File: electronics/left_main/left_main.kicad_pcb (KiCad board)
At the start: 4 copper layers, 45 x 51 mm, 186 parts, among them IC1 AS3435-EQFM, IC2 AS3435-EQFM, J1 connectors_board, J10 right_side, J11 right_side, J12 right_side, J13 right_side, J14 right_side, J15 right_side, J16 right_side, J17 right_side, J18 right_side, J19 ear_sensor, J20 ear_sensor, J21 ear_sensor, J3 FF_MIC_L_+, J4 FF_MIC_L_-, J5 FB_MIC_L_+, J6 FB_MIC_L_-, J7 HP_L_+, J8 HP_L_-, J9 right_side, SW2 reset_button, U1 BM83, U2 ATSAMD21G18_QFN, U3 MCP73831T-2ACI/OT, U4 SPX3819-3.3, U5 MAX17048G+T10, U6 AP2127K-1.8, U7 AP22814AW5, U8 AP22814AW5, Y1 32.768KHz

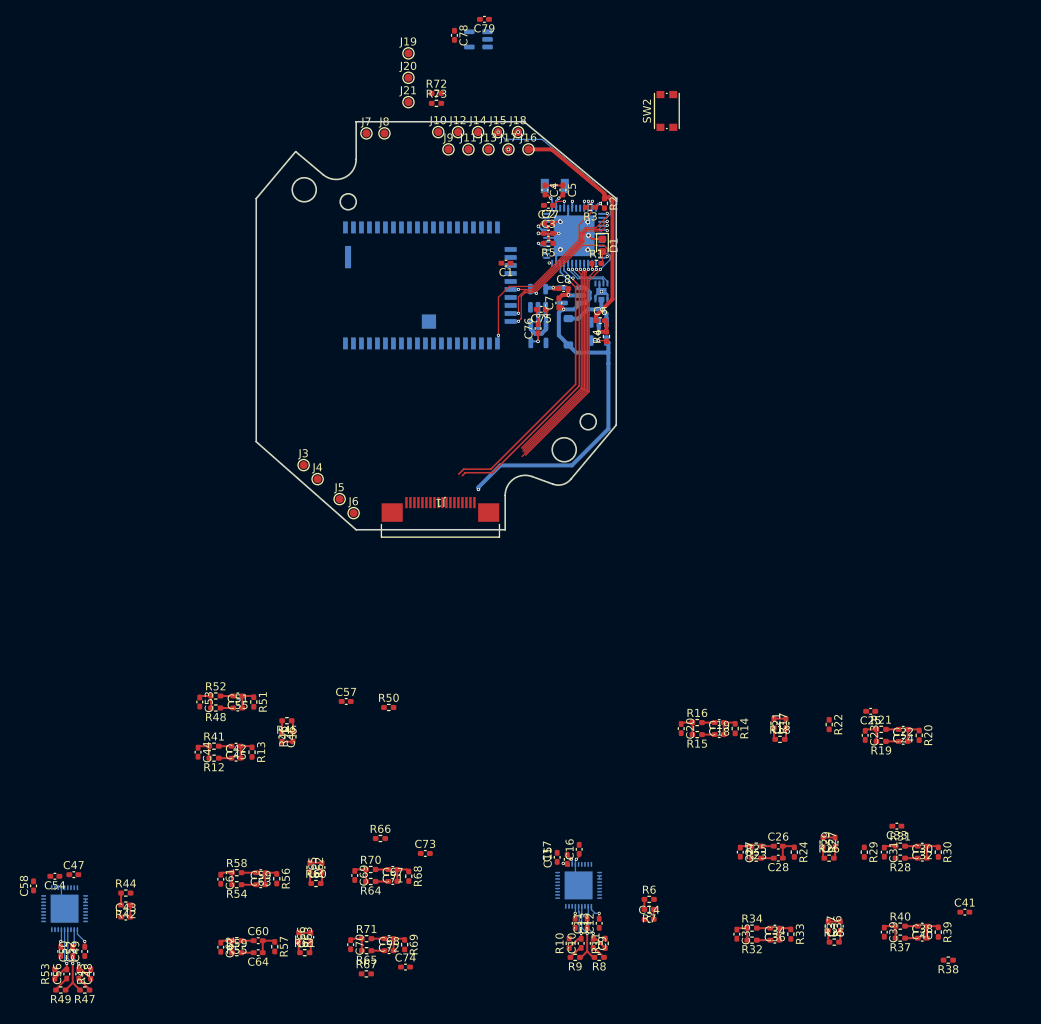
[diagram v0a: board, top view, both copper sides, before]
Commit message: L filterers + drivers layout
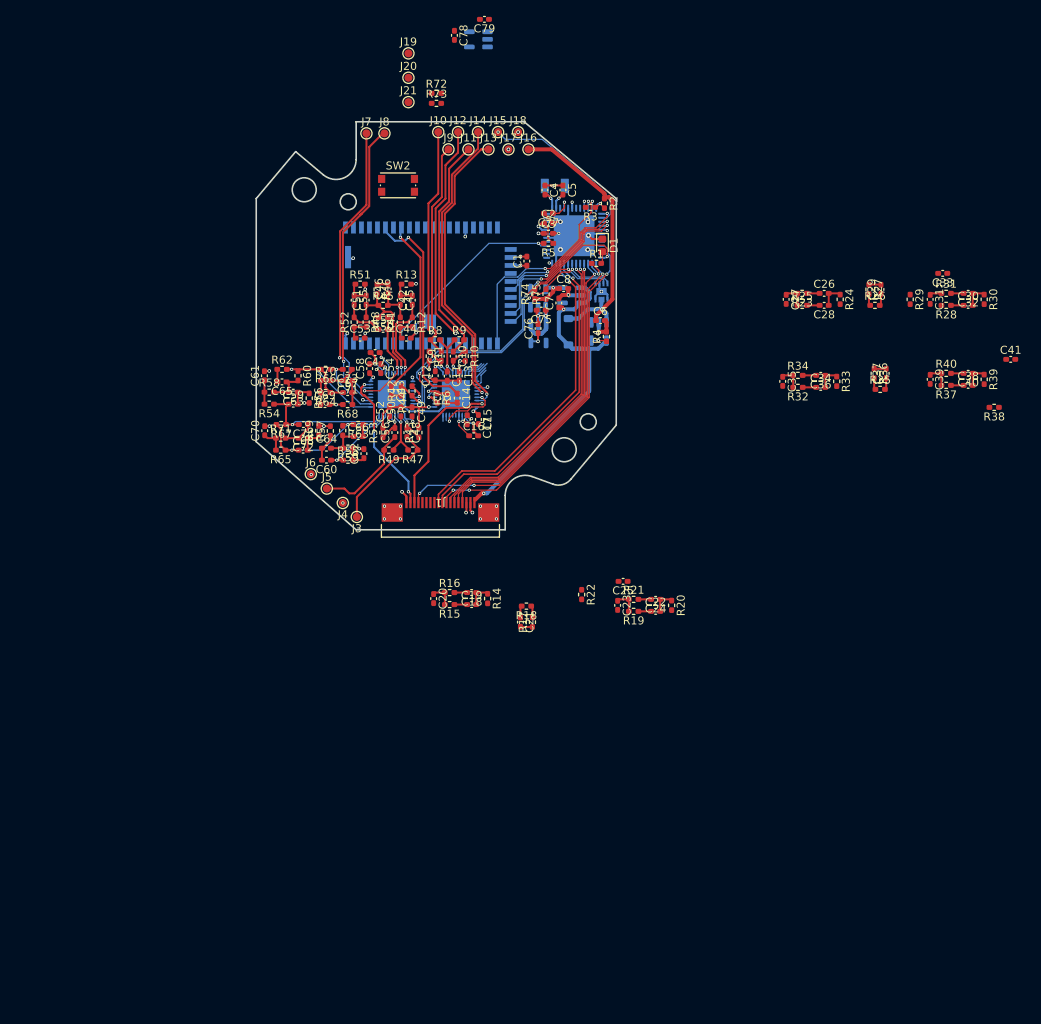
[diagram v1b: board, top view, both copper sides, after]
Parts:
- added R74: 10k, Resistor_SMD:R_0402_1005Metric_Pad0.72x0.64mm_HandSolder, F.Cu at (79.8, 50.1)
- added R75: 10k, Resistor_SMD:R_0402_1005Metric_Pad0.72x0.64mm_HandSolder, F.Cu at (81.2, 50.1)
- moved R8 79.9 mm to (67.3, 55.8), turned to 0 degrees
- moved C48 79.1 mm to (63.8, 67.4)
- moved C56 79.1 mm to (62.3, 67.4)
- moved R53 79.1 mm to (60.8, 67.4)
- moved R43 79.1 mm to (65.3, 67.4)
- moved C52 79.0 mm to (61.7, 64.8), turned to 90 degrees
- moved R47 79.0 mm to (64.5, 69.6)
- moved R49 79.0 mm to (61.5, 69.6)
- moved C50 79.0 mm to (63.1, 64.8)
- moved C49 78.9 mm to (64.5, 64.8), turned to -90 degrees
- moved R9 78.5 mm to (70.3, 55.8), turned to 0 degrees
- moved C58 77.1 mm to (59.1, 59.4)
- moved R11 76.6 mm to (66.6, 57.9), turned to -90 degrees
- moved IC2 76.2 mm to (61.9, 62.6)
- moved C9 75.8 mm to (68.1, 57.9), turned to 90 degrees
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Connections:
- J1 pad 10: /ANC_PBO -> /USB_D-
- J1 pad 11: /ANC_OFF -> /D2
- J1 pad 12: /ANC_ON -> /ANC_PBO
- J1 pad 13: /D10 -> /ANC_OFF
- J1 pad 14: /USB_D+ -> /ANC_ON
- J1 pad 15: /USB_D- -> /D10
- J1 pad 19: (no net) -> GND
- J1 pad 20: (no net) -> GND
- J1 pad 9: /D2 -> /USB_D+
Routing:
- net GND: track 33.0 -> 134.3 mm, vias 12 -> 49
- net /HP_L_-: track 0.00 -> 37.5 mm, vias 0 -> 1
- net /HP_R_+: track 0.00 -> 37.4 mm, vias 0 -> 1
- net /HP_R_-: track 0.00 -> 37.2 mm, vias 0 -> 1
- net /HP_L_+: track 0.00 -> 35.9 mm, vias 0 -> 1
- net /I2C_SDA: track 6.10 -> 39.6 mm, vias 1 -> 4
- net /I2C_SCL: track 6.17 -> 39.5 mm, vias 1 -> 2
- net /AOHPR: track 0.00 -> 27.6 mm, vias 0 -> 1
- net /FB_mic_R_+: track 1.84 -> 28.6 mm
- net /FF_mic_R_+: track 1.84 -> 27.2 mm
- net /~{RESET}: track 1.81 -> 25.3 mm
- net /AOHPL: track 0.00 -> 23.5 mm, vias 0 -> 1
- net /audio_in_R: track 0.00 -> 18.9 mm, vias 0 -> 1
- net /audio_in_L: track 0.00 -> 18.4 mm, vias 0 -> 3
- net /HP_driver_L/IOP2R: track 3.05 -> 21.3 mm, vias 0 -> 1
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- added copper zone on In2.Cu, net +1V8
- added copper zone on In2.Cu, net +3V3

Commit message: drc happy, silkscreens everywhere
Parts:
- added J22: ear_sensor, TestPoint:TestPoint_Pad_D1.0mm, F.Cu at (61.7, 29.8)
- moved C41 66.5 mm to (73.1, 51.5), turned to 180 degrees
- moved R38 65.6 mm to (73.2, 50.0), turned to 0 degrees
- moved R39 61.8 mm to (75.9, 46.0), turned to 0 degrees
- moved C38 60.3 mm to (75.2, 47.9), turned to 90 degrees
- moved C40 58.5 mm to (76.7, 47.9), turned to -90 degrees
- moved R37 57.1 mm to (75.2, 50.6), turned to -90 degrees
- moved C33 56.8 mm to (75.4, 60.2), turned to 90 degrees
- moved R31 56.6 mm to (76.4, 63.8)
- moved C32 56.5 mm to (79.2, 63.8)
- moved C31 56.1 mm to (74.4, 62.9), turned to 90 degrees
- moved R30 56.0 mm to (81.3, 63.0), turned to 90 degrees
- moved R28 55.9 mm to (76.4, 62.2)
- moved C30 55.8 mm to (79.2, 62.3)
- moved R40 55.3 mm to (76.7, 50.6), turned to 90 degrees
- moved C39 53.9 mm to (75.9, 52.6), turned to 0 degrees
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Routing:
- net /A4: track 0.88 -> 33.0 mm
- net /A2: track 0.00 -> 29.1 mm, vias 0 -> 1
- net GND: track 134.3 -> 161.5 mm, vias 49 -> 62
- net /A3: track 0.88 -> 25.7 mm, vias 1 -> 2
- net /~{RESET}: track 25.3 -> 46.5 mm, vias 1 -> 2
- net Net-(IC1-IOP1L): track 3.72 -> 20.3 mm, vias 0 -> 1
- net /HP_driver_R/IOP1R: track 5.96 -> 20.4 mm, vias 0 -> 1
- net /HP_driver_R/QOP1R: track 4.52 -> 18.0 mm, vias 0 -> 1
- net Net-(IC1-QMICR): track 4.71 -> 14.9 mm, vias 0 -> 1
- net Net-(IC1-MIXR): track 8.03 -> 16.9 mm, vias 2 -> 3
- net /HP_driver_R/IOP2R: track 5.21 -> 12.3 mm, vias 0 -> 1
- net Net-(U8-OUT): track 0.00 -> 4.94 mm, vias 0 -> 1
- net Net-(IC1-QMICL): track 2.35 -> 6.08 mm, vias 0 -> 1
- net Net-(C40-Pad2): track 1.59 -> 5.24 mm
- net Net-(C32-Pad2): track 1.59 -> 5.19 mm
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
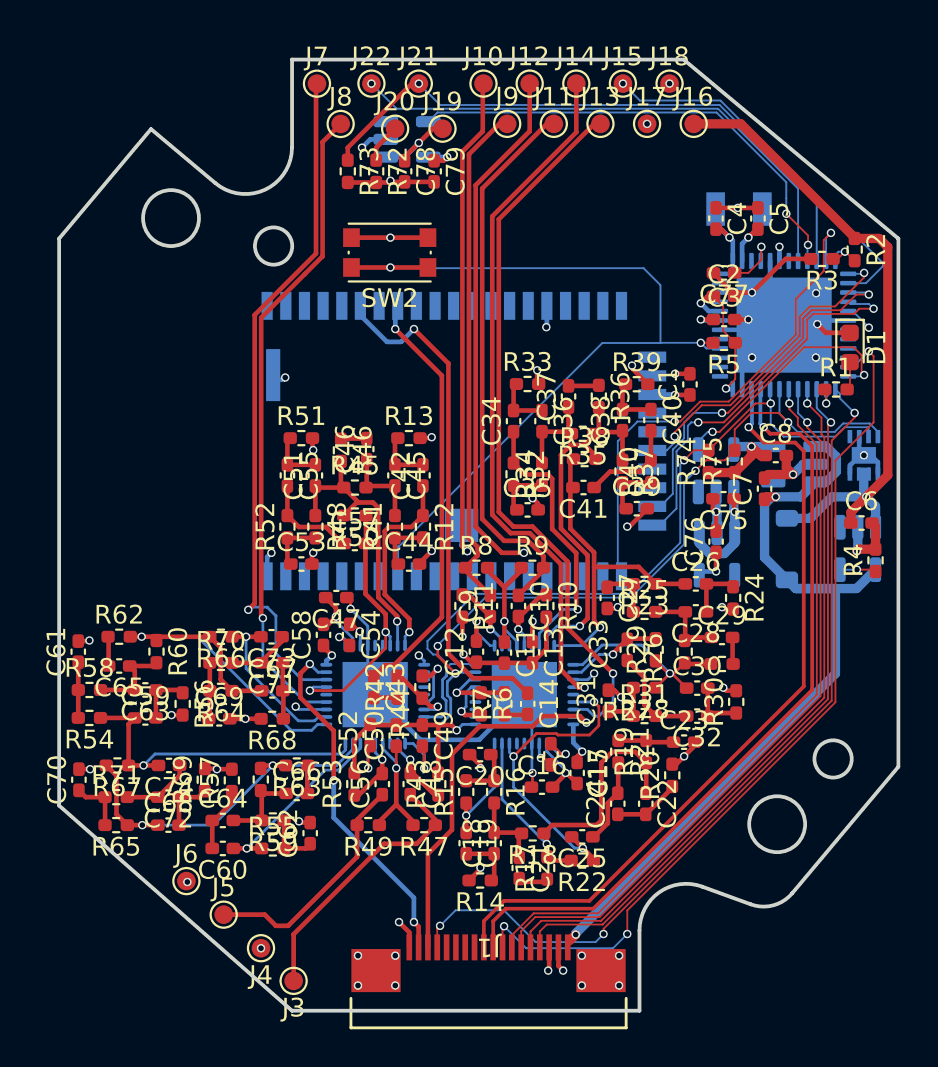
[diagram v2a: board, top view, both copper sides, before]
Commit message: silkscreen fixed
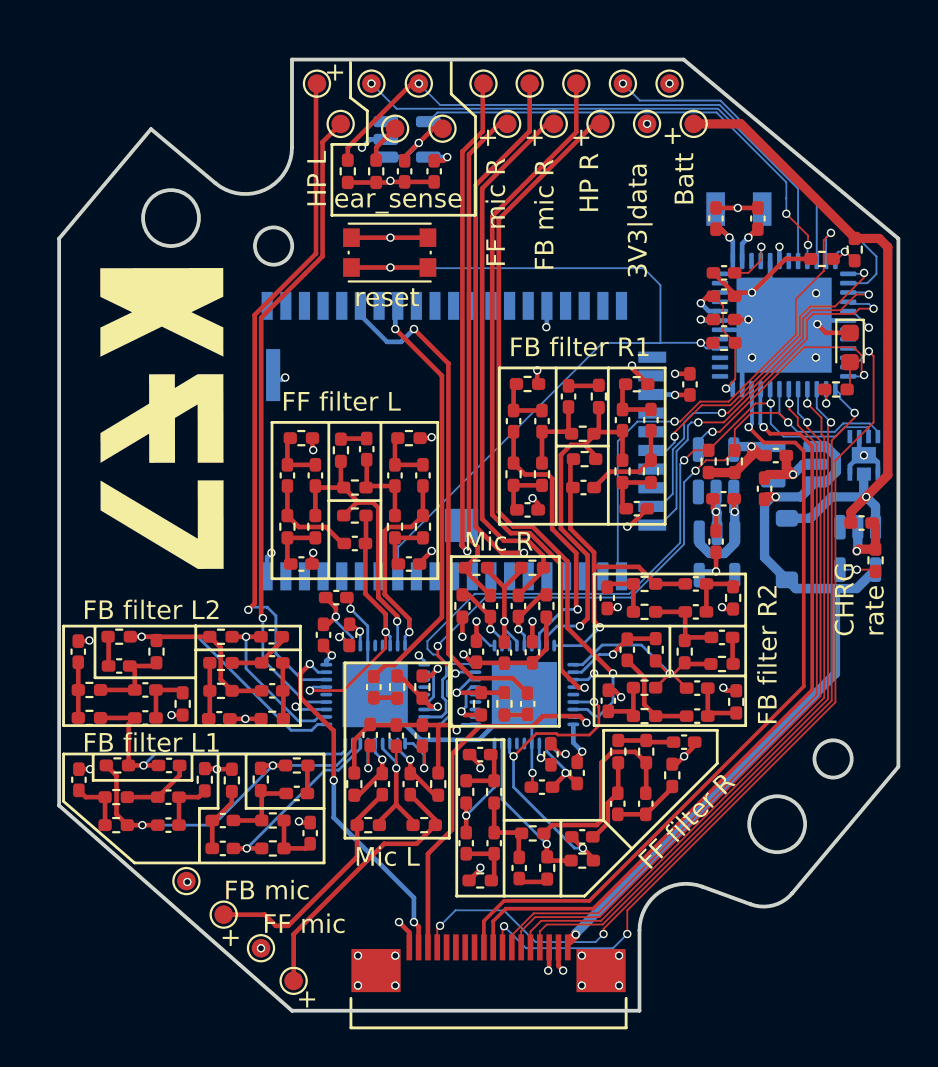
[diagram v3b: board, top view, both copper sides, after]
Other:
- board text added: "+"
- board text added: "3V3|data"
- board text added: "Batt"
- board text added: "CHRG rate"
- board text added: "FB filter L1"
- board text added: "FB filter L2"
- board text added: "FB filter R1"
- board text added: "FB filter R2"
- board text added: "FB mic"
- board text added: "FB mic R"
- board text added: "FF filter L"
- board text added: "FF filter R"
- board text added: "FF mic"
- board text added: "FF mic R"
- board text added: "HP L"
- board text added: "HP R"
- board text added: "Mic L"
- board text added: "Mic R"
- board text added: "ear_sense"
- board text added: "reset"
